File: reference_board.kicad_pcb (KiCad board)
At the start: 2 copper layers, 34 x 25 mm, 21 parts, among them J1 CONN_02X04, U1 TMP236, U2 LM399, U3 LT1001

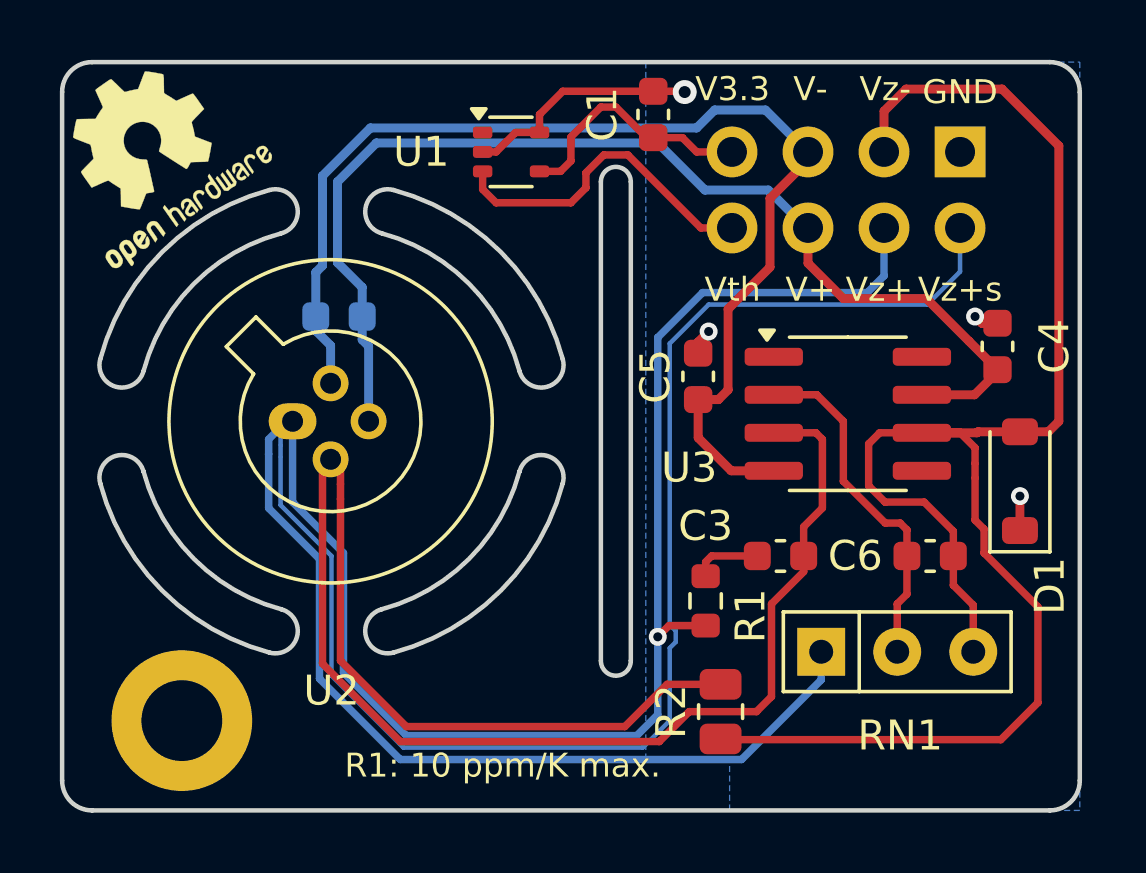
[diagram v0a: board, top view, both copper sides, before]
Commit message: Update/connector (#1)
* Replaced connector J1 with Molex SlimStack 53307-1071.

- Updated to KiCAD 10
- Changed BAS116 diode D1 footprint to SOD-123F due to availability of parts
- Added QED logo
- Removed most references to LM399. The ADR1399 is now the default. LM399 is mentioned as option.
- Added more details for different zener voltage configurations
- Added WEEE logo
- Fixed label on silkscreen refering to R1 instead of R2. It now reads 'R2: 10 ppm/K max.'

* Change standoff to WE 9774045151R.

* Changed silkscreen colour to black

* Bump version to 4.0.0

* Updated symbol

- Added WEEE logo

* Update readme

* Updated CI
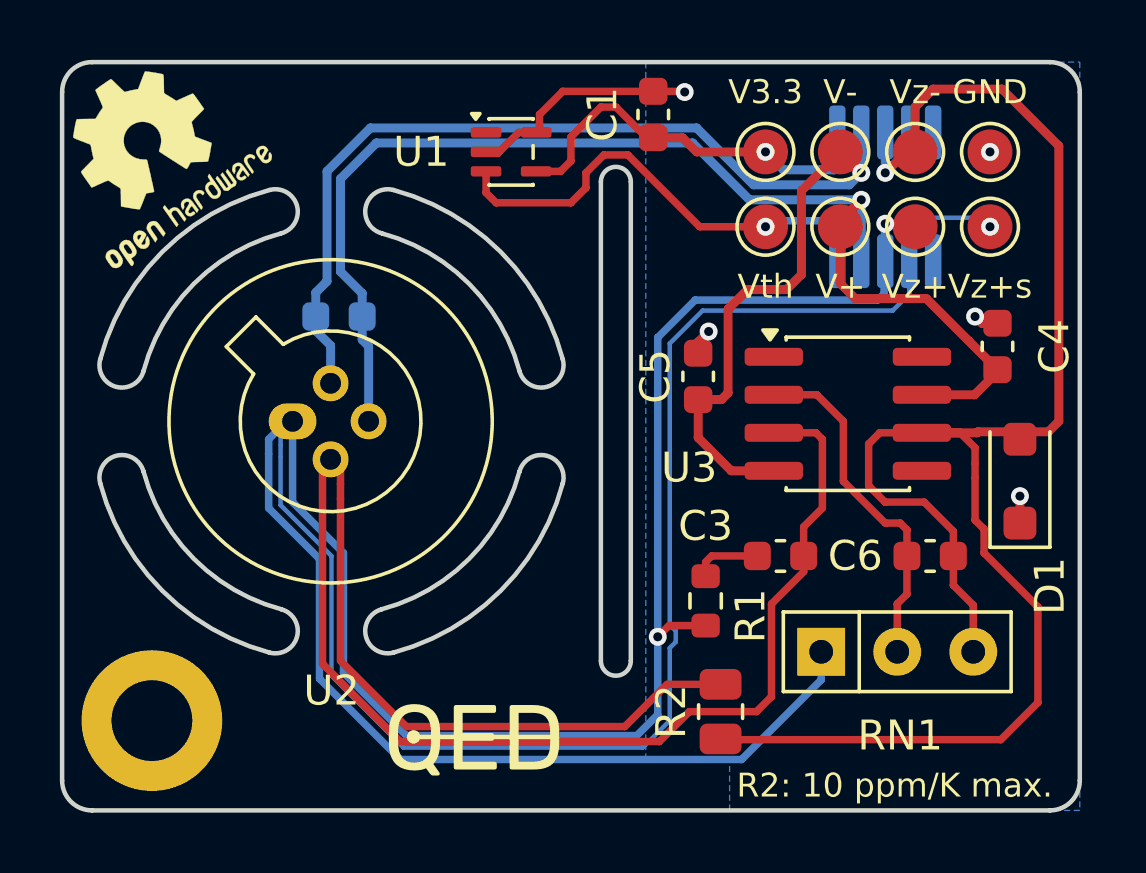
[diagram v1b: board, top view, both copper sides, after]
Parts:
- added LOGO2: Logo_QED, Custom_footprints_project:QED-logo_small, F.Cu at (113.0, 72.5)
- added SYM2: SYM_WEEE, Symbol:WEEE-Logo_4.2x6mm_SilkScreen, B.Cu at (121.5, 54.5)
- added TP1: TestPoint, TestPoint:TestPoint_Pad_D1.5mm, F.Cu at (131.0, 53.0)
- added TP2: TestPoint, TestPoint:TestPoint_Pad_D1.5mm, F.Cu at (128.5, 53.0)
- added TP3: TestPoint, TestPoint:TestPoint_Pad_D1.5mm, F.Cu at (126.0, 53.0)
- added TP4: TestPoint, TestPoint:TestPoint_Pad_D1.5mm, F.Cu at (123.5, 53.0)
- added TP5: TestPoint, TestPoint:TestPoint_Pad_D1.5mm, F.Cu at (131.0, 55.5)
- added TP6: TestPoint, TestPoint:TestPoint_Pad_D1.5mm, F.Cu at (128.5, 55.5)
- added TP7: TestPoint, TestPoint:TestPoint_Pad_D1.5mm, F.Cu at (126.0, 55.5)
- added TP8: TestPoint, TestPoint:TestPoint_Pad_D1.5mm, F.Cu at (123.5, 55.5)
- D1: footprint Diode_SMD:D_SOD-123 -> Diode_SMD:D_SOD-123F
- J1: value CONN_02X04 -> Conn_02x05_Counter_Clockwise; footprint Connector_PinSocket_2.54mm:PinSocket_2x04_P2.54mm_Vertical -> Custom_footprints_project:Molex_SlimStack_53307-1071_2x05_P0.80mm_Vertical
- U2: value LM399 -> ADR1399
- moved J1 2.92 mm to (127.5, 54.5)
- moved H1 1.00 mm to (103.0, 72.0)
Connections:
- J1 pad 3: /Vout -> /Voltage Reference/V_zener+_force
- J1 pad 4: /Voltage Reference/V_zener+_force -> /Voltage Reference/V+
- J1 pad 5: /Voltage Reference/V- -> /V_{th}
- J1 pad 6: /Voltage Reference/V+ -> /V3.3
- J1 pad 7: /V3.3 -> /Voltage Reference/V-
- J1 pad 8: Net-(J1-Pin_8) -> /Vout
- U1 pad 3: Net-(J1-Pin_8) -> /V_{th}
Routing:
- net /V_{th}: track 0.00 -> 15.9 mm, vias 0 -> 1
- net Net-(J1-Pin_8): track 11.1 -> 0.00 mm
- net /Voltage Reference/V-: track 39.4 -> 44.9 mm, vias 0 -> 1
- net /V3.3: track 8.41 -> 13.4 mm, vias 0 -> 1
- net /Voltage Reference/V+: track 37.8 -> 41.7 mm, vias 0 -> 1
- net /Zener+_sense: track 45.6 -> 47.3 mm, vias 0 -> 1
- net /Vout: track 26.2 -> 27.9 mm, vias 0 -> 1
- net /Voltage Reference/V_zener+_force: track 47.1 -> 48.2 mm, vias 1 -> 2
- net GND: track 10.9 -> 11.2 mm, vias 4 -> 5
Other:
- board text added: "ADR1399 Negative Voltage Reference"
- board text added: "Design: Patrick Baus Date: 2026-09 Version: 4.0.0"
- board text added: "R2: 10 ppm/K max."
- board text added: "Use WE 9774045151R, 4.5 mm M2.5 standoff"
- board text removed: "1.5 mm"
- board text removed: "35 µm"
- board text removed: "Copper"
- board text removed: "Core"
- board text removed: "Design: Patrick Baus Date: 2024-07 Version: 3.4.2"
- board text removed: "LM399 Negative Voltage Reference"
- board text removed: "Material"
- board text removed: "R1: 10 ppm/K max."
- board text removed: "Stackup:"
- board text removed: "Thickness"
- board text removed: "Use RAF M2106-2545-AL, 11 mm M2.5 standoff"

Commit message: Loosen design specs of the board thickness a little from +-0.13 mm to +-0.16 mm. (#3)
This change eases manufacturing and does not affect performance.
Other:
- board text added: "Manufacturing Instruction: - Material FR-4 - Finished thickness: 1.57 mm ± 0.16 mm - Surface finish: ENIG - PCBs must be RoHS compliant - Do not edit artwork, e.g. to add logos or order numbers - Clean to meet IPC J-STD-001E, Class 3 after assembly"
- board text removed: "Manufacturing Instruction: - Material FR-4 - Finished thickness: 1.57 mm ± 0.13 mm - Surface finish: ENIG - PCBs must be RoHS compliant - Do not edit artwork, e.g. to add logos or order numbers - Clean to meet IPC J-STD-001E, Class 3 after assembly"
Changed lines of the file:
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@@
 		)
 	)
-	(gr_text "Manufacturing Instruction:\n- Material FR-4\n- Finished thickness: 1.57 mm ± 0.13 mm\n- Surface finish: ENIG\n- PCBs must be RoHS compliant\n- Do not edit artwork, e.g. to add logos\n   or order numbers\n- Clean to meet IPC J-STD-001E, Class 3\n   after assembly"
+	(gr_text "Manufacturing Instruction:\n- Material FR-4\n- Finished thickness: 1.57 mm ± 0.16 mm\n- Surface finish: ENIG\n- PCBs must be RoHS compliant\n- Do not edit artwork, e.g. to add logos\n   or order numbers\n- Clean to meet IPC J-STD-001E, Class 3\n   after assembly"
 		(at 181.75 43.5 0)
 		(layer "Cmts.User")
